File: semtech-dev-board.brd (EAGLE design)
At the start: 73 x 66 mm, 66 parts, among them P2 SMAJ716-ND, P3 SMAJ716-ND, P4 SMAJ716-ND, Q1 BSS123, U1 MIC5219 3.3V, U2 QUALCOMM-TDK_B3710, U3 QUALCOMM-TDK_B3588, U4 SEMTECH_SX1236, Y1 32MHz

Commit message: added holes
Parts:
- added U$10, U$8, U$9: (no value), holes:3,0
- moved U$5 14.9 mm to (2.50, 25.2)
- moved U$3 4.20 mm to (2.40, 45.7)
- moved U$7 2.00 mm to (2.50, 41.2)
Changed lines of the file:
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@@
 <element name="U$1" library="oresat-eagle" package="SCOPE_CLIP" value="" x="2.6" y="31.8"/>
 <element name="U$2" library="oresat-eagle" package="SCOPE_CLIP" value="" x="2.5" y="36.2"/>
-<element name="U$3" library="oresat-eagle" package="SCOPE_CLIP" value="" x="2.5" y="49.9"/>
+<element name="U$3" library="oresat-eagle" package="SCOPE_CLIP" value="" x="2.4" y="45.7"/>
 <element name="U$4" library="oresat-eagle" package="SCOPE_CLIP" value="" x="2.7" y="4.4"/>
-<element name="U$5" library="oresat-eagle" package="SCOPE_CLIP" value="" x="2.5" y="10.3"/>
+<element name="U$5" library="oresat-eagle" package="SCOPE_CLIP" value="" x="2.5" y="25.2"/>
 <element name="U$6" library="oresat-eagle" package="SCOPE_CLIP" value="" x="2.5" y="19.9"/>
-<element name="U$7" library="oresat-eagle" package="SCOPE_CLIP" value="" x="2.5" y="43.2"/>
+<element name="U$7" library="oresat-eagle" package="SCOPE_CLIP" value="" x="2.5" y="41.2"/>
+<element name="U$8" library="holes" library_urn="urn:adsk.eagle:library:237" package="3,0" value="" x="4.3" y="51.9"/>
+<element name="U$9" library="holes" library_urn="urn:adsk.eagle:library:237" package="3,0" value="" x="60" y="33.8"/>
+<element name="U$10" library="holes" library_urn="urn:adsk.eagle:library:237" package="3,0" value="" x="4.5" y="11.8"/>
 </elements>
 <signals>

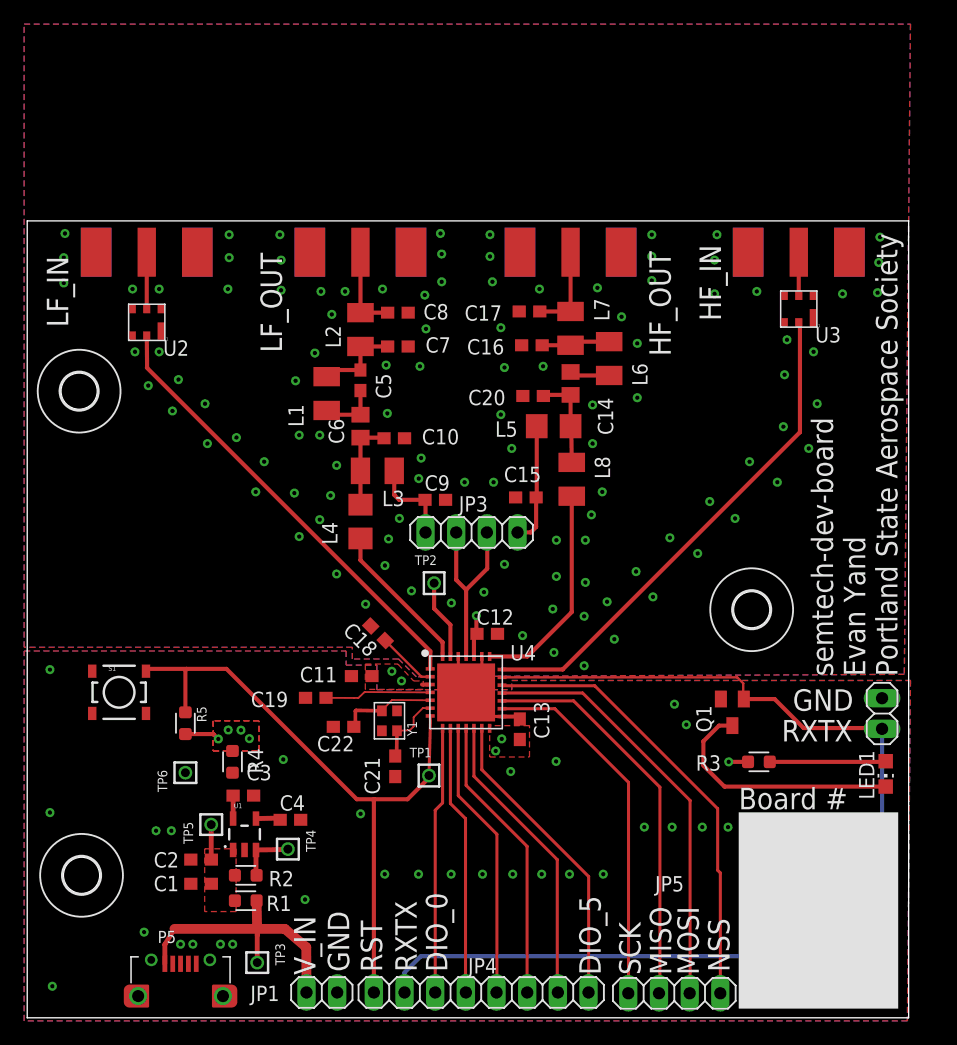
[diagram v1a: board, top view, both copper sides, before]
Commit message: Board clean up from Evan's excellent first draft. Fixed SMA connectors, SAW filters, and 1236 packages. Made sure passives were from rlc_custom. More stiching, isolate on polygons, added a mounting hole, made it more symmetric, and rounded off board to mm. Needs one more review, but needs a check in before then.
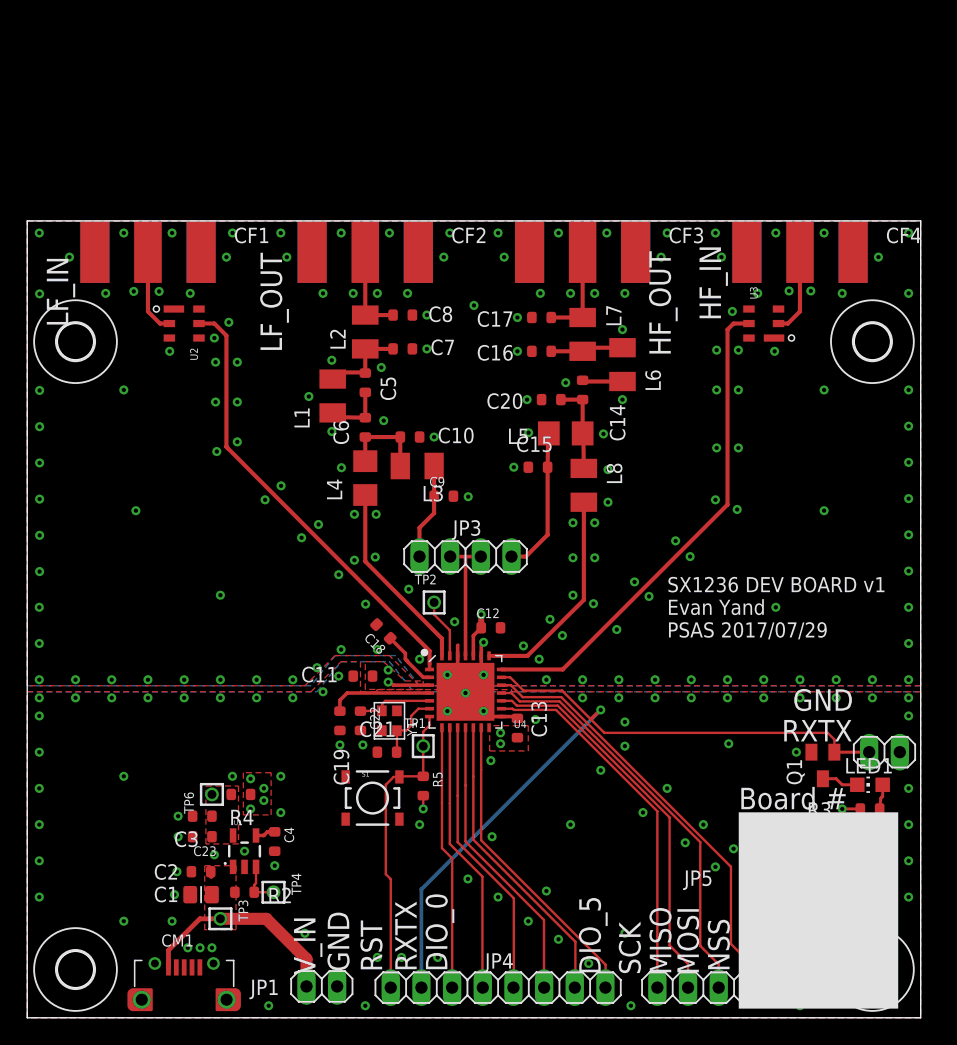
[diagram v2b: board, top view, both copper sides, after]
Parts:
- removed P2, P3, P4, RFO_LF_IN: SMAJ716-ND, psas_c3_team05:SMAJ716-ND
- removed P5: (no value), psas_c3_team05:USB-MICRO-B-PTH-HIROSE
- removed R1: 0, rcl_custom:.0603-A
- removed TP5: TEST-POINT, low-gain-radio:2MM-TEST-POINT
- removed U$4: (no value), oresat-eagle:SCOPE_CLIP
- added C23: 100nF, rcl_custom:.0603-B-NOSILK
- added CF1, CF2, CF3, CF4: 142-0701-806, psas_c3_team05:SMAJ716-ND
- added CM1: (no value), psas_c3_team05:USB-MICRO-B-PTH-HIROSE
- added U$11: (no value), holes:3,0
- added U$12, U$13, U$14, U$15: (no value), oresat-eagle:SCOPE_CLIP
- C1: device rcl_custom:C0603 -> rcl_custom:.0805-B
- C10, C11, C12, C13, C15, C16, C17, C18, C19, C2, C20, C21, C22, C3, C4, C5, C7, C8, C9: device rcl_custom:C0603 -> rcl_custom:.0603-B-NOSILK
- C14, C6: device rcl:C0805 -> rcl_custom:.0603-B-NOSILK
- R2, R3: value 0 -> 1k; device rcl_custom:.0603-A -> rcl_custom:.0603-B-NOSILK
- R4, R5: device rcl_custom:.0603-A -> rcl_custom:.0603-B-NOSILK
- U2, U3: device low-gain-radio:DCC6C -> low-gain-radio:DCC6C-EPCOS
- moved U$7 71.4 mm to (72.0, 25.0)
- moved U$2 69.7 mm to (72.0, 31.0)
- moved U$9 24.3 mm to (70.0, 56.0)
- moved S1 22.7 mm to (28.6, 18.2)
- moved R5 20.4 mm to (32.8, 19.2)
- moved R3 9.99 mm to (69.8, 17.3)
- moved U$6 9.91 mm to (2.00, 10.0)
- moved Q1 8.70 mm to (65.9, 20.9)
- moved U$10 7.82 mm to (4.00, 4.00)
- moved U3 5.16 mm to (61.0, 57.5), turned to 90 degrees
- moved TP3 4.74 mm to (16.0, 8.20)
- moved U4 4.67 mm to (36.3, 26.9)
- moved U$8 4.11 mm to (4.00, 56.0)
- moved C3 3.80 mm to (14.5, 16.7), turned to 180 degrees
- moved TP4 3.76 mm to (20.4, 10.4)
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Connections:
- removed net RFI_HF_ANT: P4.P$3, U3.P$5
- removed net RFI_LF_ANT: RFO_LF_IN.P$3, U2.P$5
- removed net VREG_IN: C1.1, C2.1, R1.2, R2.2, TP5.1, U1.1
- new net N$2: CF4.P$3, U3.2
- new net N$4: CF1.P$3, U2.2
- net GND: now also C23.2, CF1.GND1, CF1.GND2, CF1.GND3, CF1.GND4, CF2.GND1, CF2.GND2, CF2.GND3, CF2.GND4, CF3.GND1, CF3.GND2, CF3.GND3, CF3.GND4, CF4.GND1, CF4.GND2, CF4.GND3, CF4.GND4, CM1.5, U2.1, U2.3, U2.4, U2.6, U3.1, U3.3, U3.4, U3.6, U4.PAD; no longer P2.GND1, P2.GND2, P2.GND3, P2.GND4, P3.GND1, P3.GND2, P3.GND3, P3.GND4, P4.GND1, P4.GND2, P4.GND3, P4.GND4, P5.5, RFO_LF_IN.GND1, RFO_LF_IN.GND2, RFO_LF_IN.GND3, RFO_LF_IN.GND4, U2.P$1, U2.P$3, U2.P$4, U2.P$6, U3.P$1, U3.P$3, U3.P$4, U3.P$6, U4.0
- net RFI_HF: now also U3.5; no longer U3.P$2
- net RFI_LF: now also U2.5; no longer U2.P$2
- net RFO_HF_OUT: now also CF3.P$3; no longer P3.P$3
- net RFO_LF_OUT: now also CF2.P$3; no longer P2.P$3
- net VREG_OUT: now also C23.1
- net V_IN: now also C1.1, C2.1, CM1.1, R2.2, U1.1; no longer P5.1, R1.1
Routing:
- net SX1236_RST: track 53.5 -> 25.5 mm
- net RXTX: track 89.2 -> 63.9 mm, vias 0 -> 1
- net LED-: track 20.8 -> 3.06 mm
- net LED+: track 9.62 -> 2.07 mm
- net N$4: track 0.00 -> 7.09 mm
- net N$2: track 0.00 -> 7.09 mm
- net V_IN: track 23.5 -> 18.0 mm
- net GND: track 12.1 -> 6.76 mm, vias 138 -> 242
- net VR_PA: track 16.1 -> 10.8 mm
- net RFI_LF_ANT: track 4.68 -> 0.00 mm
- net RFI_HF_ANT: track 3.58 -> 0.00 mm
- net RFO_LF: track 12.6 -> 15.9 mm
- net VREG_IN: track 2.91 -> 0.00 mm
- net HFO_PA_HEAD: track 10.1 -> 12.3 mm
- net VREG_OUT: track 2.05 -> 0.00 mm
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- added copper zone on layer 1, net VREG_OUT
- added copper zone on layer 1, net V_IN
- removed copper zone on layer 1, net VREG_IN
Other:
- board size 73 x 66 mm -> 74 x 66 mm
- board text added: "SX1236 DEV BOARD v1 Evan Yand PSAS 2017/07/29"
- board text removed: "semtech-dev-board Evan Yand Portland State Aerospace Society"

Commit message: TNAMES cleanup, better ground plane splitting - probably TOTALLY unnecessary on this board, but whatevs, it's fun. Updated SX1236 symbol, switched digital/analog caps to be correct.
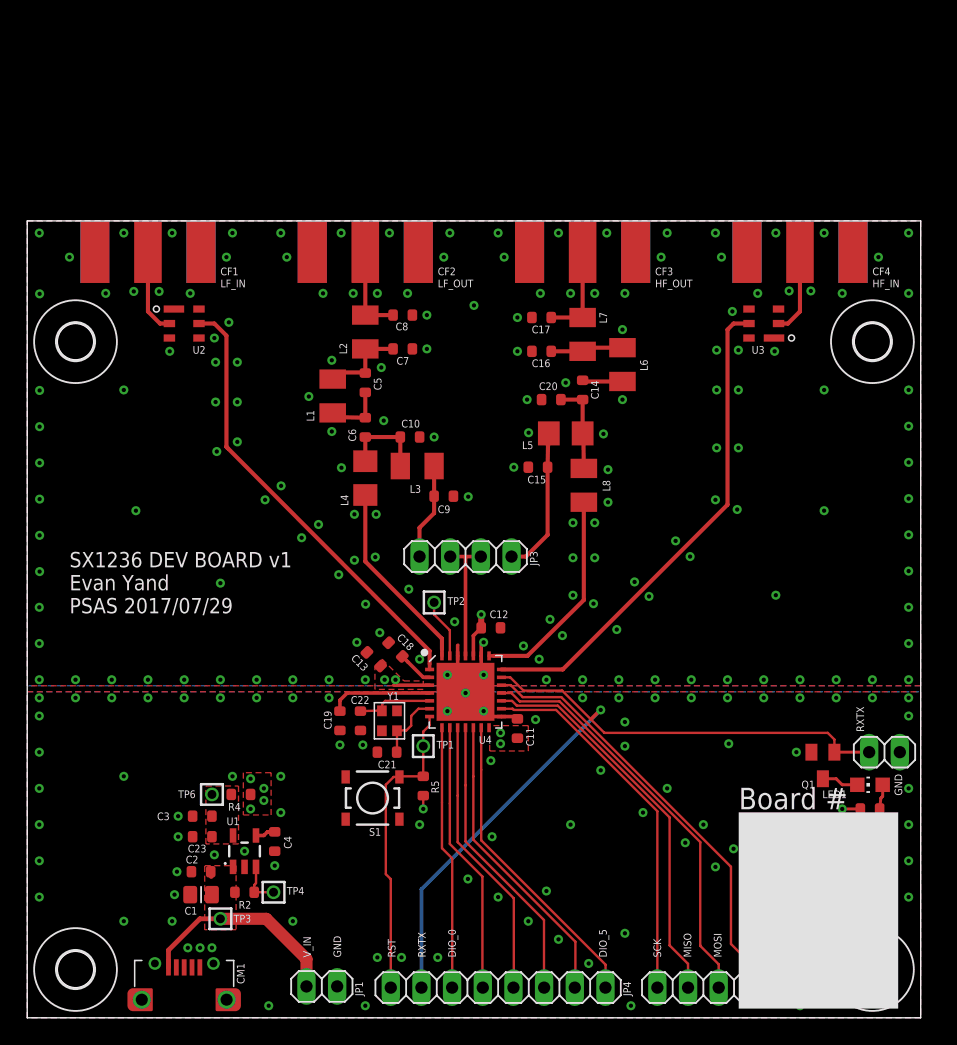
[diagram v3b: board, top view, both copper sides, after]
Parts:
- moved C11 13.5 mm to (40.6, 24.0), turned to 90 degrees
- moved C13 13.2 mm to (28.7, 29.7), turned to 135 degrees
- moved C18 1.80 mm to (30.5, 30.5)
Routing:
- net VR_ANA: track 4.89 -> 2.98 mm
- net +3V3: track 9.78 -> 9.27 mm

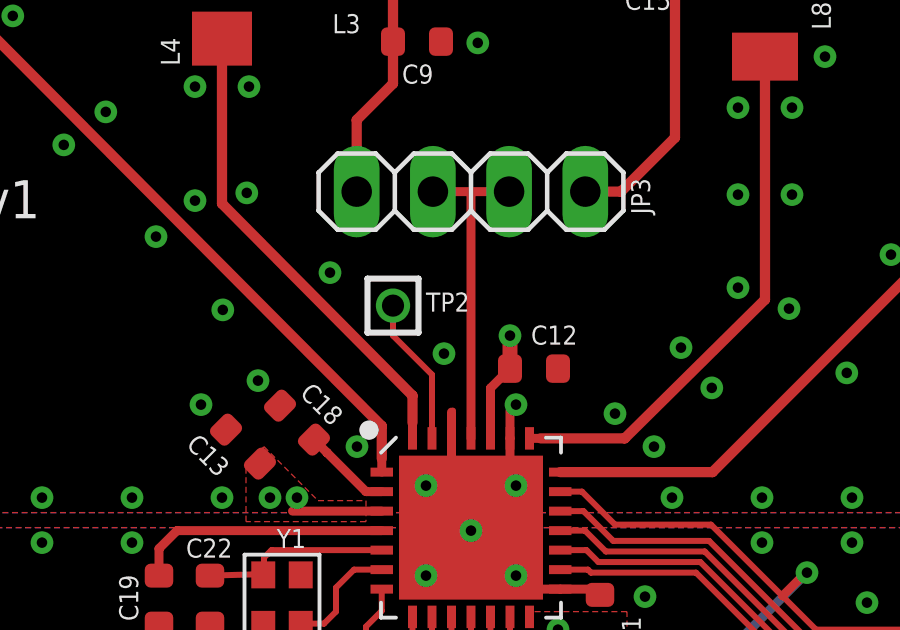
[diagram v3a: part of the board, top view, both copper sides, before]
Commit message: Added cap to VR_PA, because it said to. Probably overkill, given the other ones.
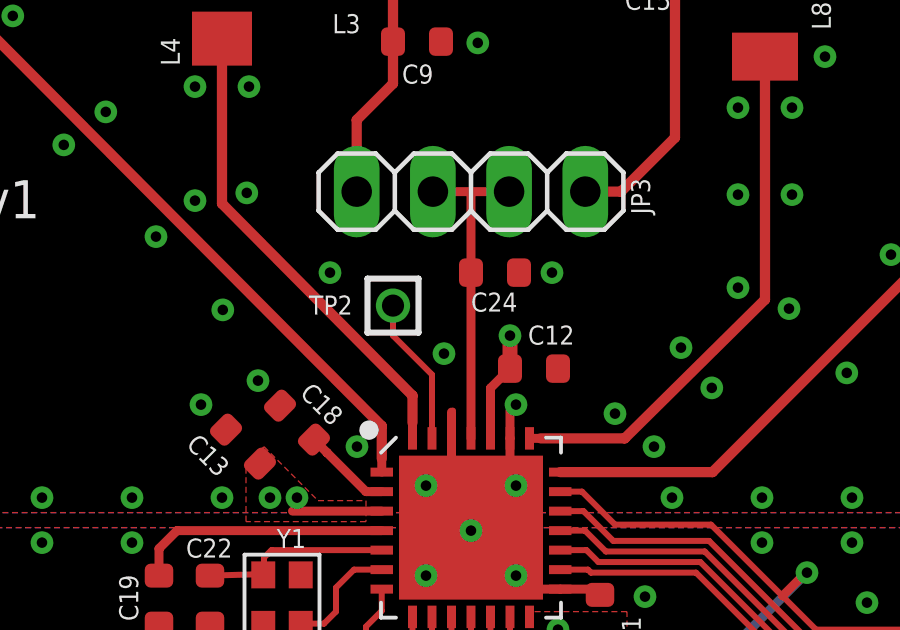
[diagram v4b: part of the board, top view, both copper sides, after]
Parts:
- added C24: 100nF, rcl_custom:.0603-B-NOSILK
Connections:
- net GND: now also C24.2
- net VR_PA: now also C24.1
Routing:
- net GND: vias 242 -> 243
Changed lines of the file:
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@@
 <setting verticaltext="up"/>
 </settings>
-<grid distance="0.5" unitdist="mm" unit="mm" style="lines" multiple="1" display="yes" altdistance="0.02" altunitdist="mm" altunit="mm"/>
+<grid distance="0.1" unitdist="mm" unit="mm" style="lines" multiple="1" display="yes" altdistance="0.02" altunitdist="mm" altunit="mm"/>
 <layers>
 <layer number="1" name="Top" color="4" fill="1" visible="yes" active="yes"/>
@@
 <layer number="23" name="tOrigins" color="15" fill="1" visible="yes" active="yes"/>
 <layer number="24" name="bOrigins" color="15" fill="1" visible="yes" active="yes"/>
-<layer number="25" name="tNames" color="7" fill="1" visible="yes" active="yes"/>
+<layer number="25" name="tNames" color="7" fill="1" visible="no" active="yes"/>
 <layer number="26" name="bNames" color="7" fill="1" visible="no" active="yes"/>
 <layer number="27" name="tValues" color="7" fill="1" visible="no" active="yes"/>
@@
 </element>
 <element name="C12" library="rcl_custom" package=".0603-B-NOSILK" value="100nF" x="38.4" y="32.3" smashed="yes">
-<attribute name="NAME" x="38.3" y="33.1" size="0.635" layer="25" font="vector" ratio="20"/>
+<attribute name="NAME" x="38.2" y="33.1" size="0.635" layer="25" font="vector" ratio="20"/>
 <attribute name="NAME" x="38.4" y="32.3" size="0.3" layer="33" ratio="15" align="center"/>
 <attribute name="VALUE" x="37.2" y="30.7" size="0.8" layer="27" font="vector" ratio="15"/>
@@
 </element>
 <element name="TP2" library="low-gain-radio" package="2MM-TEST-POINT" value="TEST-POINT" x="33.7" y="34.4" smashed="yes">
-<attribute name="NAME" x="34.8" y="34.2" size="0.635" layer="25" font="vector" ratio="20"/>
+<attribute name="NAME" x="30.9" y="34.1" size="0.635" layer="25" font="vector" ratio="20"/>
 </element>
 <element name="U4" library="low-gain-radio" package="QFN28" value="SEMTECH_SX1236" x="36.3" y="26.9" smashed="yes">
@@
 <attribute name="NAME" x="70" y="61.5" size="0.635" layer="25" font="vector" ratio="20"/>
 <attribute name="VALUE" x="71.112" y="61.876" size="1.27" layer="27" font="vector" ratio="20"/>
+</element>
+<element name="C24" library="rcl_custom" package=".0603-B-NOSILK" value="100nF" x="37.1" y="35.5" smashed="yes">
+<attribute name="NAME" x="36.3" y="34.2" size="0.635" layer="25" font="vector" ratio="20"/>
+<attribute name="NAME" x="37.1" y="35.5" size="0.3" layer="33" ratio="15" align="center"/>
+<attribute name="VALUE" x="35.9" y="33.9" size="0.8" layer="27" font="vector" ratio="15"/>
 </element>
 </elements>
@@
 <wire x1="39.275" y1="24.95" x2="40.408575" y2="24.95" width="0.3" layer="1"/>
 <wire x1="40.408575" y1="24.95" x2="40.599996875" y2="24.758578125" width="0.3" layer="1"/>
+<contactref element="C24" pad="2"/>
+<via x="39" y="35.5" extent="1-16" drill="0.35"/>
 </signal>
 <signal name="SPI_NSS">
@@
 <contactref element="JP3" pad="2"/>
 <contactref element="JP3" pad="3"/>
-<wire x1="36.3" y1="38.2" x2="36.3" y2="29.975" width="0.3" layer="1"/>
-<wire x1="36.3" y1="38.2" x2="37.57" y2="38.2" width="0.3" layer="1"/>
+<wire x1="37.57" y1="38.2" x2="36.3" y2="38.2" width="0.3" layer="1"/>
 <wire x1="35.03" y1="38.2" x2="36.3" y2="38.2" width="0.3" layer="1"/>
+<contactref element="C24" pad="1"/>
+<wire x1="36.3" y1="35.5" x2="36.3" y2="29.975" width="0.3" layer="1"/>
+<wire x1="36.3" y1="35.5" x2="36.3" y2="38.2" width="0.3" layer="1"/>
 </signal>
 <signal name="RFO_HF_OUT">

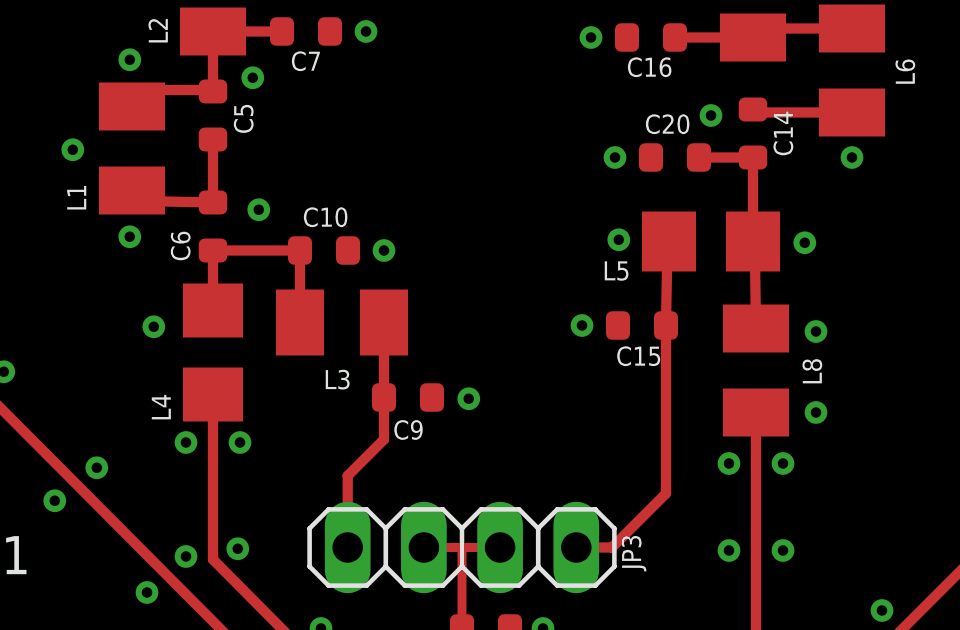
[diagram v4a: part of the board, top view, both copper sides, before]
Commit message: Added updated BOM, and adjusted inductor sizes
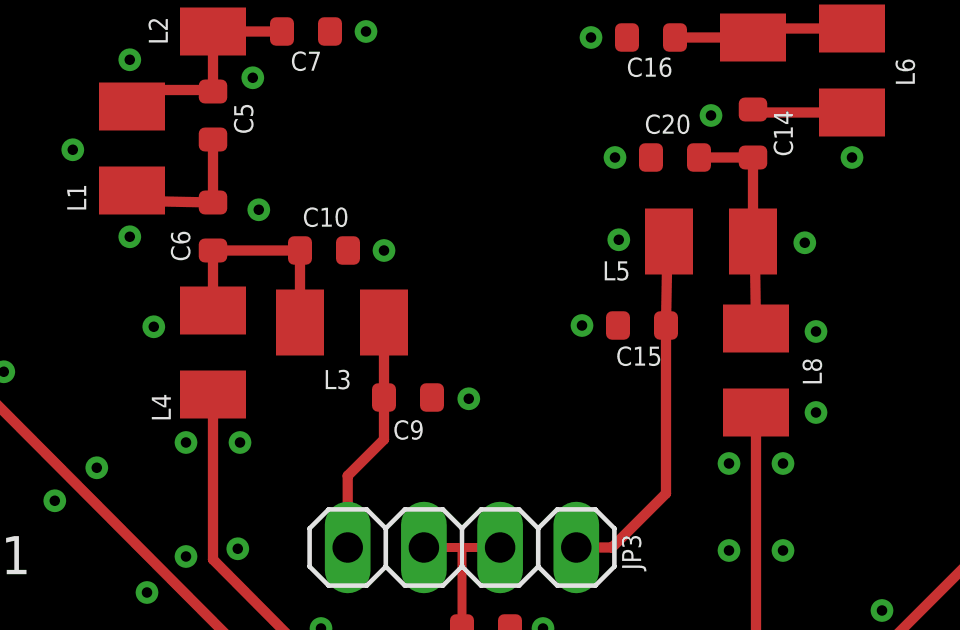
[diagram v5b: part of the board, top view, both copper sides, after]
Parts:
- L4, L5: device rcl:L3225P -> rcl:L3225M
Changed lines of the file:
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@@
 <attribute name="VALUE" x="30.395" y="42.525" size="1.27" layer="27"/>
 </element>
-<element name="L5" library="rcl" library_urn="urn:adsk.eagle:library:334" package="L3225P" value="33nH" x="44.6" y="48.4" smashed="yes" rot="R180">
+<element name="L5" library="rcl" library_urn="urn:adsk.eagle:library:334" package="L3225M" value="33nH" x="44.6" y="48.4" smashed="yes" rot="R180">
 <attribute name="NAME" x="40.981" y="47.105" size="0.635" layer="25" font="vector" ratio="20"/>
 <attribute name="VALUE" x="46.505" y="51.575" size="1.27" layer="27" rot="R180"/>
 </element>
-<element name="L4" library="rcl" library_urn="urn:adsk.eagle:library:334" package="L3225P" value="10nH" x="28" y="44.7" smashed="yes" rot="R90">
+<element name="L4" library="rcl" library_urn="urn:adsk.eagle:library:334" package="L3225M" value="10nH" x="28" y="44.7" smashed="yes" rot="R90">
 <attribute name="NAME" x="26.595" y="42.395" size="0.635" layer="25" font="vector" ratio="20" rot="R90"/>
 <attribute name="VALUE" x="31.175" y="42.795" size="1.27" layer="27" rot="R90"/>
